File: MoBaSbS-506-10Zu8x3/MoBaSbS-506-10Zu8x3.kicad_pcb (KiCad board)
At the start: 2 copper layers, 57.8 x 21.6 mm, 11 parts, among them J1 Conn_02x05_Odd_Even, J2 5, J3 1, J4 2, J5 6, J6 3, J7 7, J8 4, J9 8

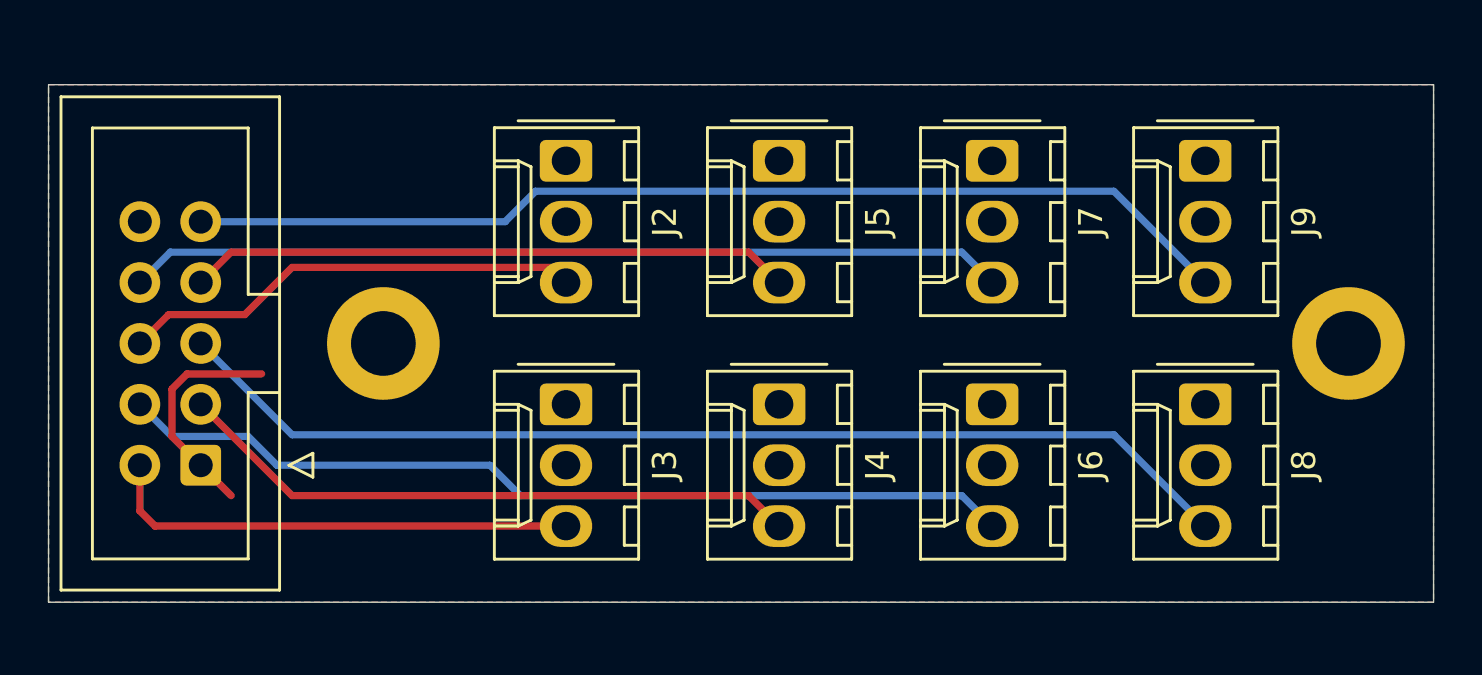
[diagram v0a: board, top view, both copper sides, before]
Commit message: Generated panels, added some new PCBs
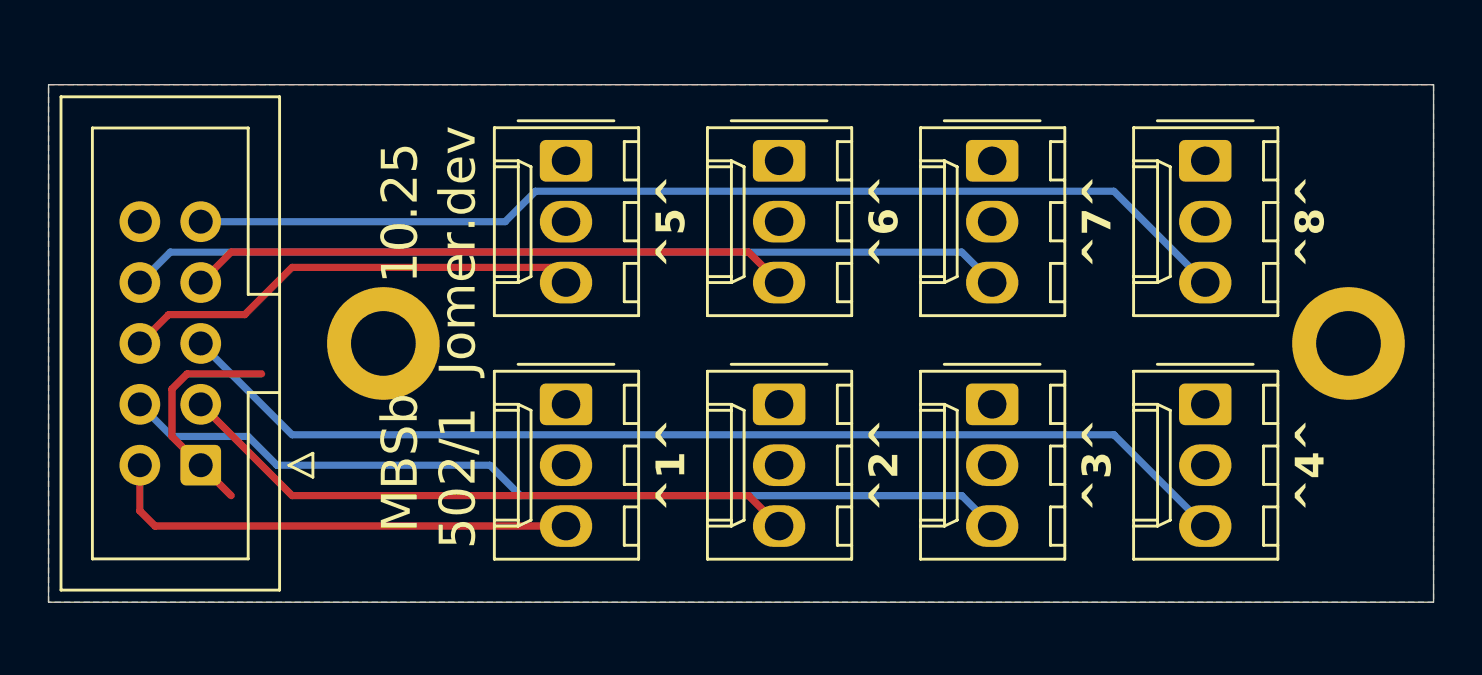
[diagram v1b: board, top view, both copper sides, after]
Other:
- board text added: "MBSb 10.25 502/1 Jomer.dev"
- board text added: "^1^"
- board text added: "^2^"
- board text added: "^3^"
- board text added: "^4^"
- board text added: "^5^"
- board text added: "^6^"
- board text added: "^7^"
- board text added: "^8^"
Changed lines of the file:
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@@
 			(at 2.54 -4.12 270)
 			(layer "F.SilkS")
+			(hide yes)
 			(effects
 				(font
@@
 			(at 2.54 -4.12 270)
 			(layer "F.SilkS")
+			(hide yes)
 			(effects
 				(font
@@
 			(at 2.54 -4.12 270)
 			(layer "F.SilkS")
+			(hide yes)
 			(effects
 				(font
@@
 			(at 2.54 -4.12 270)
 			(layer "F.SilkS")
+			(hide yes)
 			(effects
 				(font
@@
 			(at 2.54 -4.12 270)
 			(layer "F.SilkS")
+			(hide yes)
 			(effects
 				(font
@@
 			(at 2.54 -4.12 270)
 			(layer "F.SilkS")
+			(hide yes)
 			(effects
 				(font
@@
 			(at 2.54 -4.12 270)
 			(layer "F.SilkS")
+			(hide yes)
 			(effects
 				(font
@@
 			(at 2.54 -4.12 270)
 			(layer "F.SilkS")
+			(hide yes)
 			(effects
 				(font
@@
 		(layer "Edge.Cuts")
 	)
+	(gr_text "^4^"
+		(at 141.605 93.98 90)
+		(layer "F.SilkS")
+		(effects
+			(font
+				(size 1.2 1.2)
+				(thickness 0.3)
+				(bold yes)
+			)
+			(justify bottom)
+		)
+	)
+	(gr_text "^8^"
+		(at 141.605 83.82 90)
+		(layer "F.SilkS")
+		(effects
+			(font
+				(size 1.2 1.2)
+				(thickness 0.3)
+				(bold yes)
+			)
+			(justify bottom)
+		)
+	)
+	(gr_text "^6^"
+		(at 123.825 83.82 90)
+		(layer "F.SilkS")
+		(effects
+			(font
+				(size 1.2 1.2)
+				(thickness 0.3)
+				(bold yes)
+			)
+			(justify bottom)
+		)
+	)
+	(gr_text "^7^"
+		(at 132.715 83.82 90)
+		(layer "F.SilkS")
+		(effects
+			(font
+				(size 1.2 1.2)
+				(thickness 0.3)
+				(bold yes)
+			)
+			(justify bottom)
+		)
+	)
+	(gr_text "MBSb       10.25\n502/1  Jomer.dev"
+		(at 104.14 88.646 90)
+		(layer "F.SilkS")
+		(effects
+			(font
+				(size 1.5 1.5)
+				(thickness 0.3)
+			)
+		)
+	)
+	(gr_text "^3^"
+		(at 132.715 93.98 90)
+		(layer "F.SilkS")
+		(effects
+			(font
+				(size 1.2 1.2)
+				(thickness 0.3)
+				(bold yes)
+			)
+			(justify bottom)
+		)
+	)
+	(gr_text "^5^"
+		(at 114.935 83.82 90)
+		(layer "F.SilkS")
+		(effects
+			(font
+				(size 1.2 1.2)
+				(thickness 0.3)
+				(bold yes)
+			)
+			(justify bottom)
+		)
+	)
+	(gr_text "^2^"
+		(at 123.825 93.98 90)
+		(layer "F.SilkS")
+		(effects
+			(font
+				(size 1.2 1.2)
+				(thickness 0.3)
+				(bold yes)
+			)
+			(justify bottom)
+		)
+	)
+	(gr_text "^1^"
+		(at 114.935 93.98 90)
+		(layer "F.SilkS")
+		(effects
+			(font
+				(size 1.2 1.2)
+				(thickness 0.3)
+				(bold yes)
+			)
+			(justify bottom)
+		)
+	)
 	(segment
